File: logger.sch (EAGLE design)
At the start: 69 parts, among them IC1 LTC4412, J1 POWER_JACKPTH, Q1 FDN360P, Q2 FDN360P, Q3 2N7002PW, Q4 2N7002PW, U1 FT232RL

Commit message: Vcl attached to clock power and communication
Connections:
- new net D4-SENSE_3V3_SWITCH: MCU.PD4(XCK/T0), SENSE.EN, TPS6122.EN
- net D6-CLOCK_3V3_SWITCH: no longer MCU.PD4(XCK/T0), SENSE.EN, TPS6122.EN
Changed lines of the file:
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@@
 <net name="D6-CLOCK_3V3_SWITCH" class="0">
-<segment>
-<wire x1="152.4" y1="88.9" x2="185.42" y2="88.9" width="0.1524" layer="91"/>
-<label x="154.94" y="88.9" size="1.778" layer="95"/>
-<pinref part="MCU" gate="G$1" pin="PD4(XCK/T0)"/>
-</segment>
-<segment>
-<wire x1="116.84" y1="17.78" x2="116.84" y2="15.24" width="0.1524" layer="91"/>
-<wire x1="116.84" y1="15.24" x2="83.82" y2="15.24" width="0.1524" layer="91"/>
-<label x="83.82" y="15.24" size="1.778" layer="95"/>
-<pinref part="SENSE" gate="G$1" pin="EN"/>
-</segment>
 <segment>
 <wire x1="287.02" y1="256.54" x2="287.02" y2="254" width="0.1524" layer="91"/>
@@
 <label x="154.94" y="83.82" size="1.778" layer="95"/>
 <pinref part="MCU" gate="G$1" pin="PD6(AIN0)"/>
-</segment>
-<segment>
-<pinref part="TPS6122" gate="G$1" pin="EN"/>
-<wire x1="152.4" y1="-22.86" x2="147.32" y2="-22.86" width="0.1524" layer="91"/>
-<label x="147.32" y="-22.86" size="1.778" layer="95"/>
 </segment>
 </net>
@@
 </segment>
 </net>
+<net name="D4-SENSE_3V3_SWITCH" class="0">
+<segment>
+<pinref part="TPS6122" gate="G$1" pin="EN"/>
+<wire x1="147.32" y1="-22.86" x2="167.64" y2="-22.86" width="0.1524" layer="91"/>
+<label x="152.4" y="-22.86" size="1.778" layer="95"/>
+</segment>
+<segment>
+<pinref part="MCU" gate="G$1" pin="PD4(XCK/T0)"/>
+<wire x1="152.4" y1="88.9" x2="175.26" y2="88.9" width="0.1524" layer="91"/>
+<label x="154.94" y="88.9" size="1.778" layer="95"/>
+</segment>
+<segment>
+<pinref part="SENSE" gate="G$1" pin="EN"/>
+<wire x1="116.84" y1="17.78" x2="116.84" y2="15.24" width="0.1524" layer="91"/>
+<wire x1="116.84" y1="15.24" x2="86.36" y2="15.24" width="0.1524" layer="91"/>
+<label x="86.36" y="15.24" size="1.778" layer="95"/>
+</segment>
+</net>

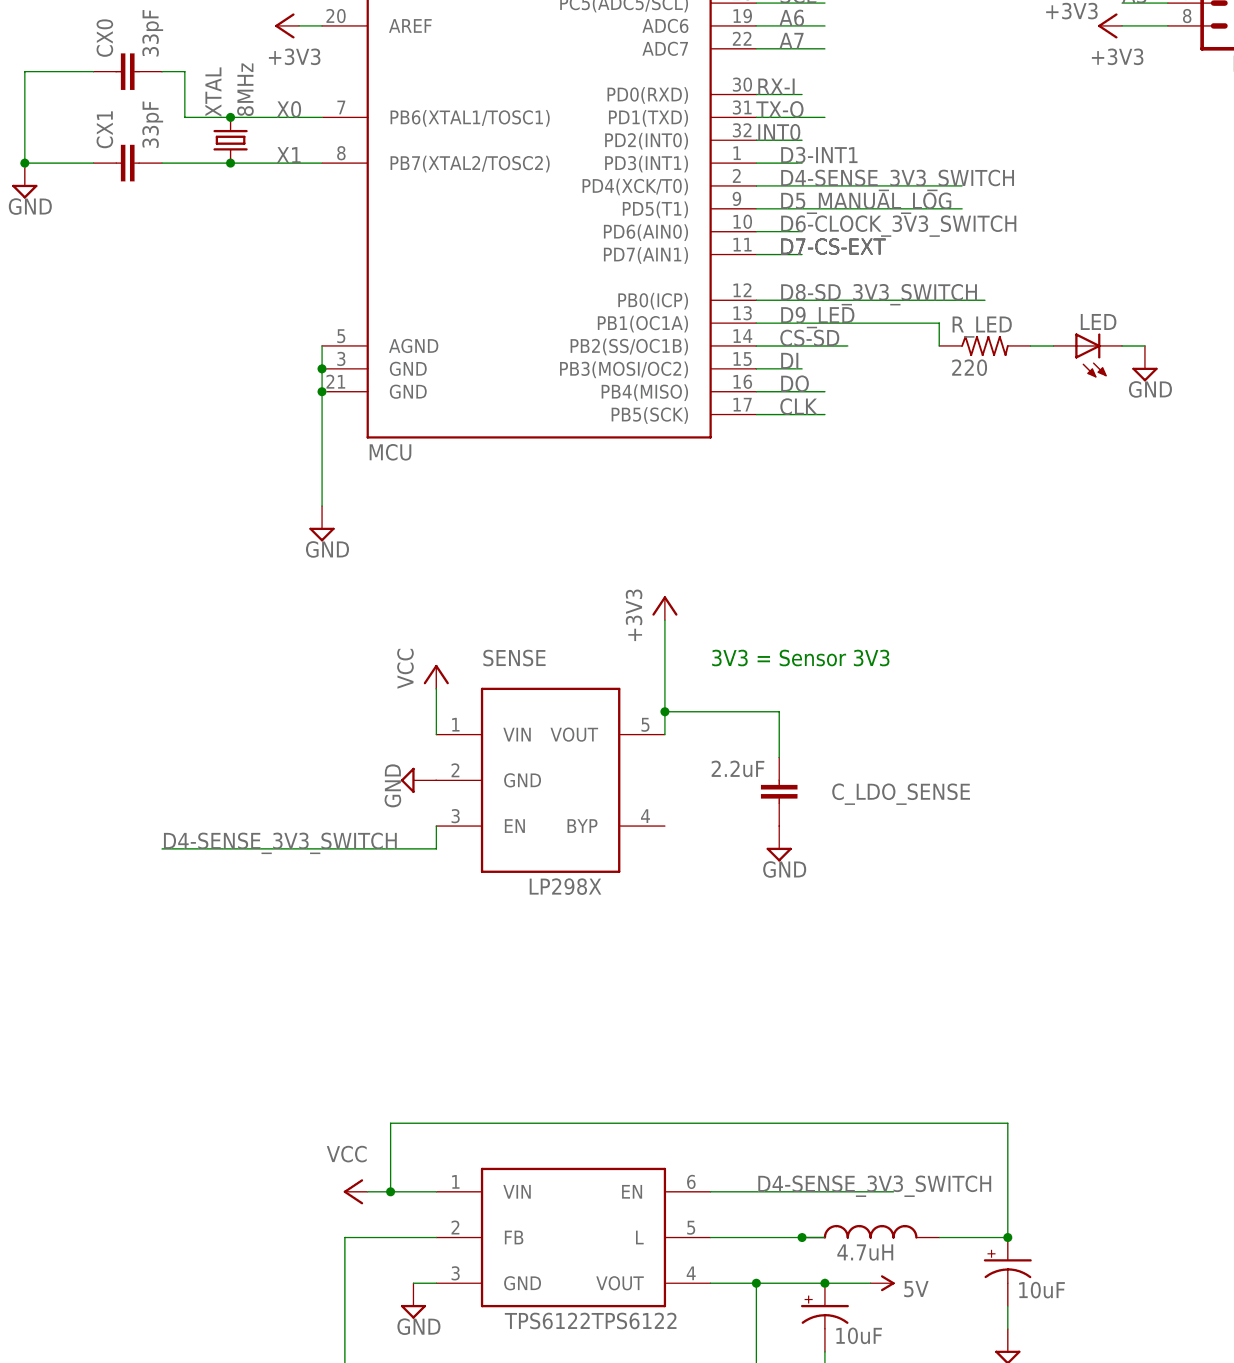
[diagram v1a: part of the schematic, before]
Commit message: Straighten traces
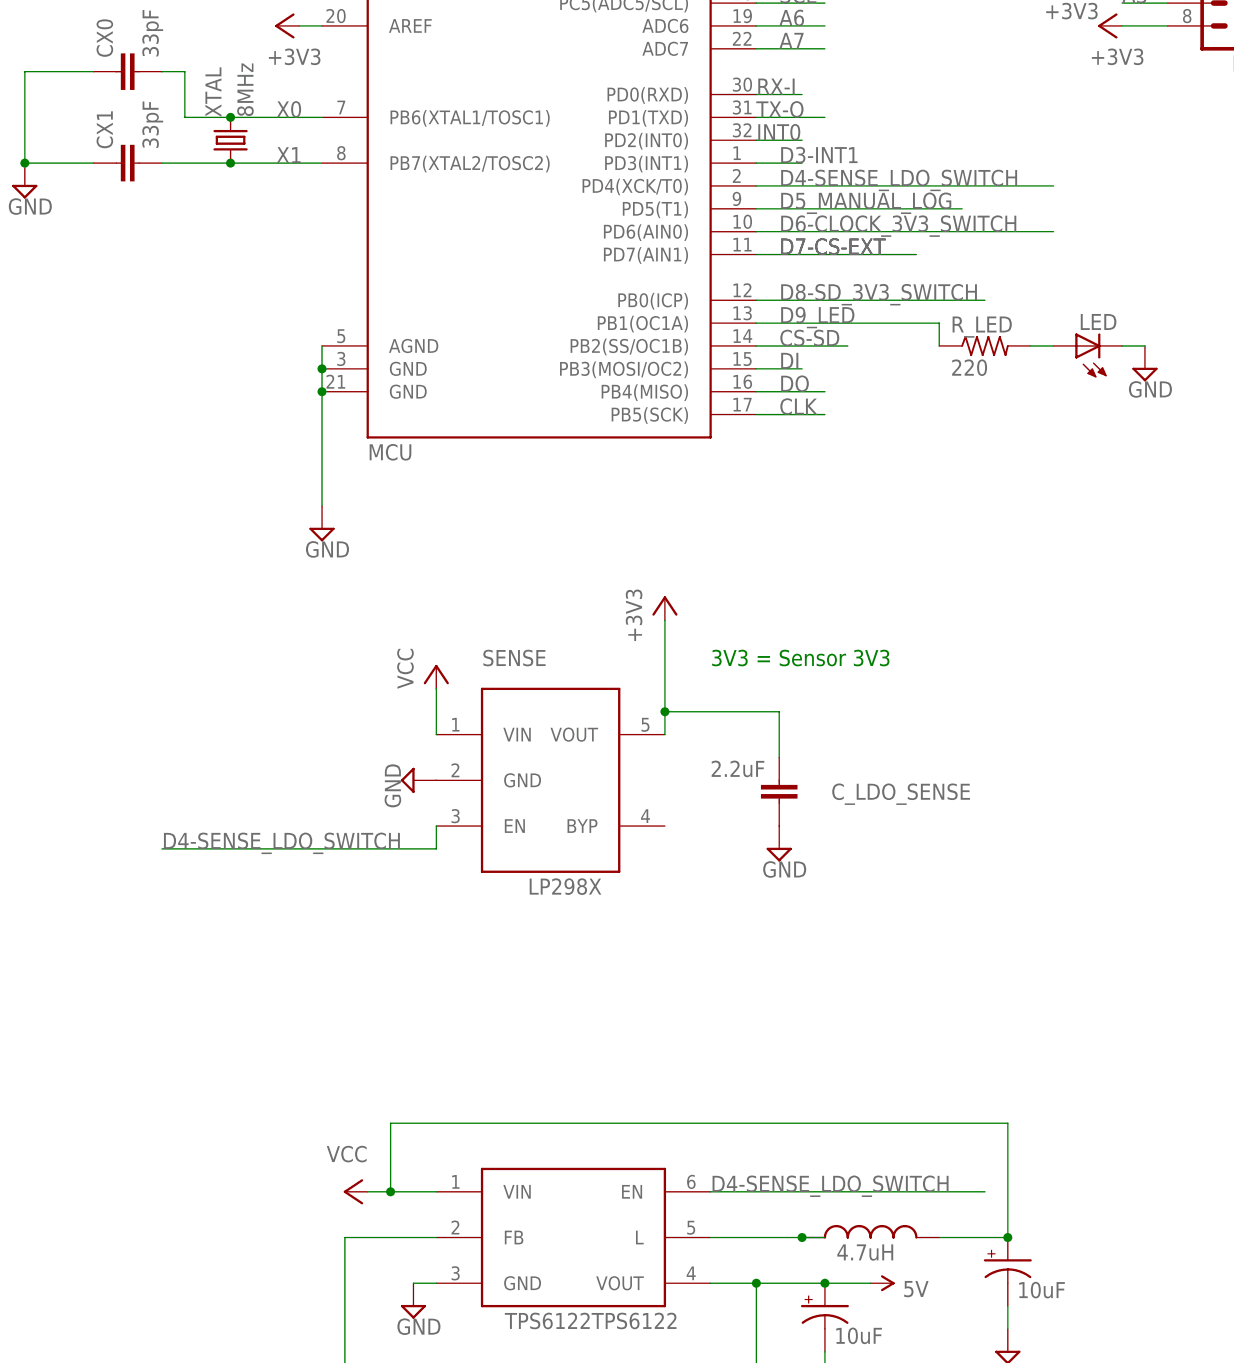
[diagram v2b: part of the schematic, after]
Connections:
- net D4-SENSE_3V3_SWITCH renamed D4-SENSE_LDO_SWITCH
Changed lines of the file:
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@@
 <net name="D7-CS-EXT" class="0">
 <segment>
-<wire x1="157.48" y1="81.28" x2="152.4" y2="81.28" width="0.1524" layer="91"/>
+<wire x1="170.18" y1="81.28" x2="152.4" y2="81.28" width="0.1524" layer="91"/>
 <label x="154.94" y="81.28" size="1.778" layer="95"/>
 <label x="154.94" y="81.28" size="1.778" layer="95"/>
@@
 </segment>
 <segment>
-<wire x1="152.4" y1="83.82" x2="157.48" y2="83.82" width="0.1524" layer="91"/>
+<wire x1="152.4" y1="83.82" x2="185.42" y2="83.82" width="0.1524" layer="91"/>
 <label x="154.94" y="83.82" size="1.778" layer="95"/>
 <pinref part="MCU" gate="G$1" pin="PD6(AIN0)"/>
@@
 </segment>
 </net>
-<net name="D4-SENSE_3V3_SWITCH" class="0">
+<net name="D4-SENSE_LDO_SWITCH" class="0">
 <segment>
 <pinref part="TPS6122" gate="G$1" pin="EN"/>
-<wire x1="147.32" y1="-22.86" x2="167.64" y2="-22.86" width="0.1524" layer="91"/>
-<label x="152.4" y="-22.86" size="1.778" layer="95"/>
+<wire x1="147.32" y1="-22.86" x2="177.8" y2="-22.86" width="0.1524" layer="91"/>
+<label x="147.32" y="-22.86" size="1.778" layer="95"/>
 </segment>
 <segment>
 <pinref part="MCU" gate="G$1" pin="PD4(XCK/T0)"/>
-<wire x1="152.4" y1="88.9" x2="175.26" y2="88.9" width="0.1524" layer="91"/>
+<wire x1="152.4" y1="88.9" x2="185.42" y2="88.9" width="0.1524" layer="91"/>
 <label x="154.94" y="88.9" size="1.778" layer="95"/>
 </segment>

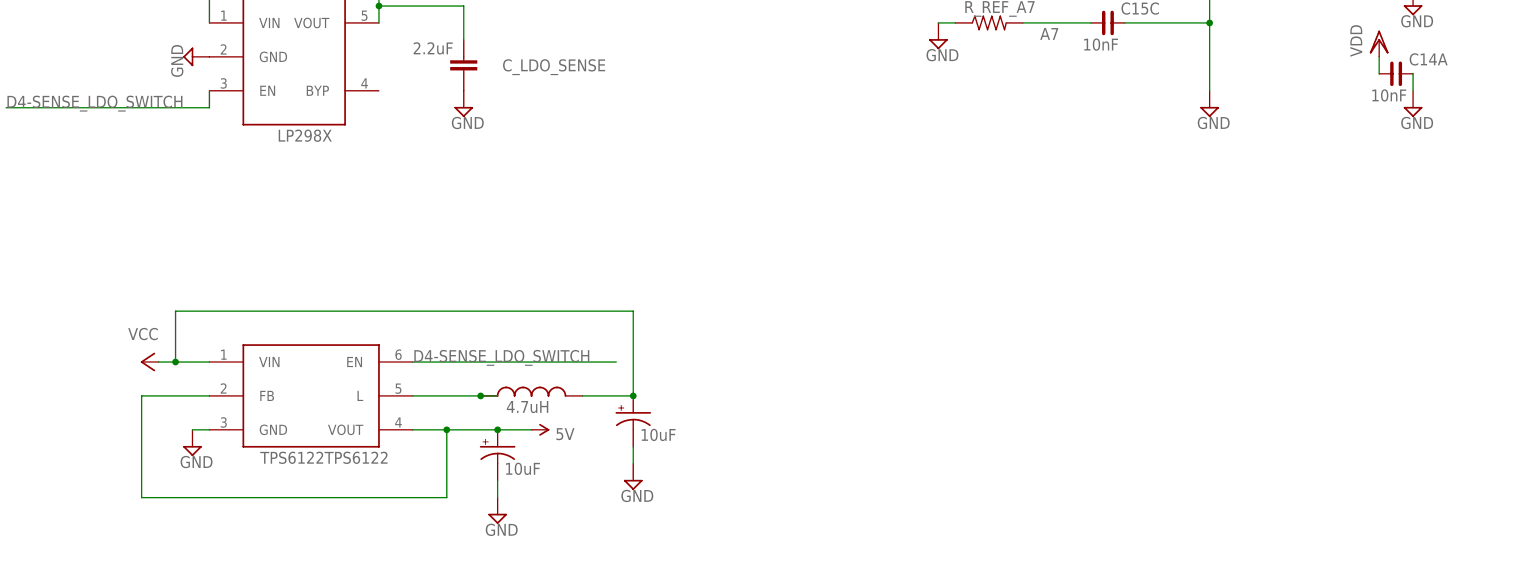
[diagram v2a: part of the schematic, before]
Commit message: Charge pump
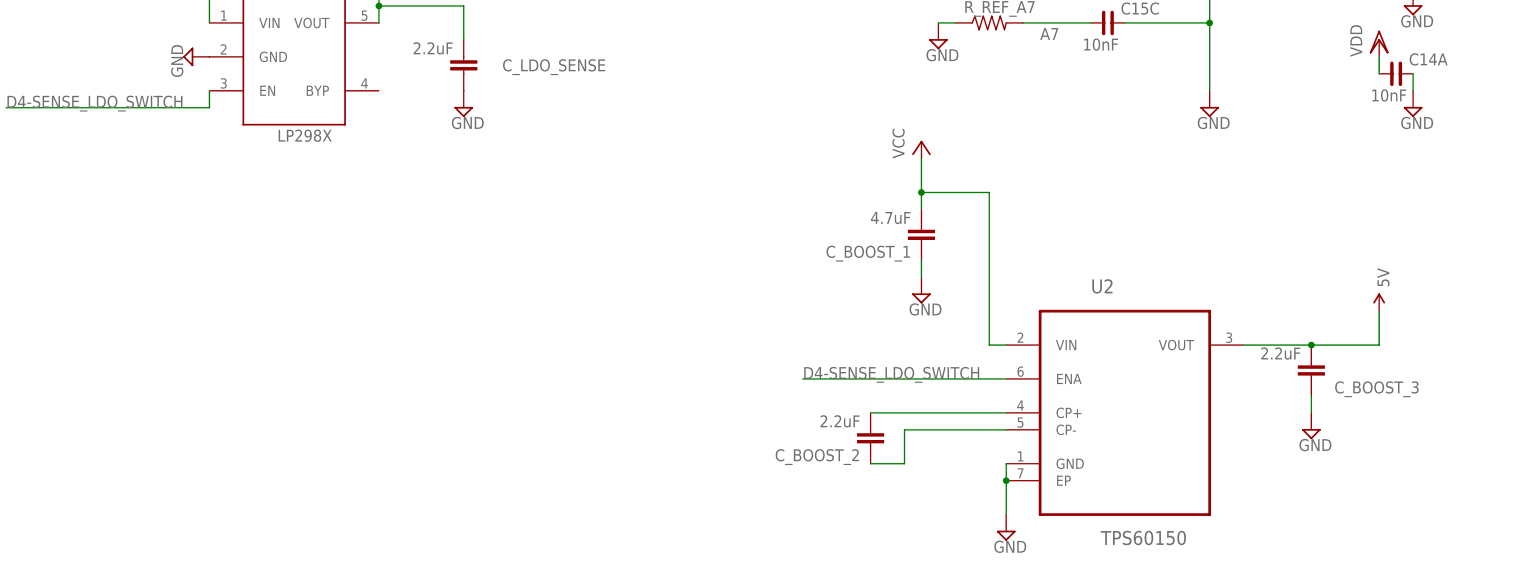
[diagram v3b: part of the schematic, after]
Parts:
- removed C1, C2: 10uF, SparkFun-Passives:CAP_POL1206
- removed L1: 4.7uH, SteveMarple:INDUCTOR1210
- removed TPS6122: TPS6122TPS6122, csandell:TPS6122TPS6122
- added C_BOOST_1: 4.7uF, resistor:C-EUC0603
- added C_BOOST_2, C_BOOST_3: 2.2uF, resistor:C-EUC0603
- added U2: TPS60150, ti_by_element14:TPS60150DRVR
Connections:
- removed net N$12: L1.1, TPS6122.L
- new net N$14: C_BOOST_2.2, U2.CP+
- new net N$15: C_BOOST_2.1, U2.CP-
- net 5V: now also C_BOOST_3.2, U2.VOUT; no longer C2.+, TPS6122.FB, TPS6122.VOUT
- net D4-SENSE_LDO_SWITCH: now also U2.ENA; no longer TPS6122.EN
- net GND: now also C_BOOST_1.1, C_BOOST_3.1, U2.EP, U2.GND; no longer C1.-, C2.-, TPS6122.GND
- net VCC: now also C_BOOST_1.2, U2.VIN; no longer C1.+, L1.2, TPS6122.VIN

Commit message: Updated BOM and board layout with cheaper and smaller component packages
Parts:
- removed C_LDO_SENSE1, DECOUP: 2.2uF, resistor:C-EUC0603
- removed RTC: DS3231SN, comfile:DS3231SN
- removed SENSE: LP2985, adafruit:LP298XS
- added 3.3_SENSE: LT1461DHS8-5PBF, LTC_By_element14_Batch_1:LT1461DHS8-5PBF
- added 5V_CHARGE_PUMP: TPS60150, ti_by_element14:TPS60150DRVR
- added C1: 0.1uF, resistor:C-EUC0603
- added CLOCK_BATT_DECOUPLE: 10uF, SparkFun-Passives:CAP_POL1206
- added CLOCK_CIN, SD_CIN, SENSE_CIN: 1uF, rcl:C-EUC0603
- added C_LDO_CLOCK: 2.2uF, resistor:C-EUC0603
- added D+, D-: 27ohm, rcl:R-US_R0603
- CLOCK_BATT_DECOUP: value 1uF -> 0.1uF
- MCU: value ATMega328 -> ATMEGA328P-MU; device SparkFun:ATMEGA168 -> Atmel_By_element14_Batch_1-00:ATMEGA328P-MU
- U1: value FT232RL -> DS3231MZ/V+T; device SparkFun-DigitalIC:FT232RL-BASICSSOP -> Maxim-DS3231MZ_8-SOIC:DS3231MZ/V+T
- U2: value TPS60150 -> FT231X-Q; device ti_by_element14:TPS60150DRVR -> FT231X:FT231X-Q
- renumbered R_REF_A0 to A0, R_REF_A1 to A1, R_REF_A2 to A2, R_REF_A3 to A3, R_REF_A6 to A6, R_REF_A7 to A7
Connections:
- new net N$13: D-.1, U2.USBDM
- new net N$16: D+.1, U2.USBDP
- new net N$17: C1.1, U2.3V3OUT, U2.RESET#, U2.VCCIO
- net +3V3: now also 3.3_SENSE.VOUT, H0.3, H0.5, H1.1, H1.3, H3.6; no longer H0.2, H0.4, H0.6, H0.8, H1.2, H1.4, H3.7, SENSE.VOUT
- net 5V: now also 5V_CHARGE_PUMP.VOUT, H3.7; no longer H3.6, U2.VOUT
- net A0: now also C14C.1, H0.2, MCU.PC0; no longer C15B.1, H0.1, MCU.PC0(ADC0)
- net A1: now also C14D.1, H0.4, MCU.PC1; no longer C15A.1, H0.3, MCU.PC1(ADC1)
- net A2: now also C15A.1, H0.6, MCU.PC2; no longer C14D.1, H0.5, MCU.PC2(ADC2)
- net A3: now also C15B.1, H0.8, MCU.PC3; no longer C14C.1, H0.7, MCU.PC3(ADC3)
- net A6: now also A6.1, C15C.2, H1.2; no longer A6.2, C15D.1, H1.1
- net A7: now also A7.1, C15D.2, H1.4; no longer A7.2, C15C.1, H1.3
- net BAT: now also CLOCK_BATT_DECOUPLE.+, U1.VBAT; no longer RTC.VBAT
- net CLK: now also MCU.PB5; no longer MCU.PB5(SCK)
- net CS-SD: now also MCU.PB2; no longer MCU.PB2(SS/OC1B)
- net D3-INT1: now also MCU.PD3; no longer MCU.PD3(INT1)
- net D4-SENSE_LDO_SWITCH: now also 3.3_SENSE.~SHDN, 5V_CHARGE_PUMP.ENA, MCU.PD4; no longer MCU.PD4(XCK/T0), SENSE.EN, U2.ENA
- net D5_MANUAL_LOG: now also MCU.PD5; no longer MCU.PD5(T1)
- net D6-CLOCK_3V3_SWITCH: now also MCU.PD6; no longer MCU.PD6(AIN0)
- net D7-CS-EXT: now also H3.5, MCU.PD7; no longer H3.4, MCU.PD7(AIN1)
- net D8-SD_3V3_SWITCH: now also MCU.PB0; no longer MCU.PB0(ICP)
- net D9_LED: now also MCU.PB1; no longer MCU.PB1(OC1A)
- net DI: now also MCU.PB3; no longer MCU.PB3(MOSI/OC2)
- net DO: now also MCU.PB4; no longer MCU.PB4(MISO)
- net DTR: now also U2.DTR#; no longer U1.DTR
- net GND: now also 3.3_SENSE.GND, 5V_CHARGE_PUMP.EP, 5V_CHARGE_PUMP.GND, A6.2, A7.2, C1.2, C15C.1, C15D.1, CLOCK_BATT_DECOUPLE.-, CLOCK_CIN.2, C_LDO_CLOCK.1, H0.1, H0.7, MCU.GND, MCU.GND_2, MCU.GND_3, SD_CIN.2, SENSE_CIN.2, U1.GND, U2.CTS#, U2.GND@13, U2.GND@21, U2.GND@3; no longer A6.1, A7.1, C15C.2, C15D.2, C_LDO_SENSE1.1, DECOUP.2, MCU.AGND, MCU.GND@1, MCU.GND@2, RTC.GND, RTC.NC1, RTC.NC2, RTC.NC3, RTC.NC4, RTC.NC5, RTC.NC6, RTC.NC7, RTC.NC8, SENSE.GND, U1.AGND, U1.CTS, U1.GND1, U1.GND2, U1.GND3, U1.TEST, U2.EP, U2.GND
- net INT0: now also MCU.PD2, U1.*INT/SQW; no longer MCU.PD2(INT0), RTC.!INT/SQW
- net N$14: now also 5V_CHARGE_PUMP.CP+; no longer U2.CP+
- net N$15: now also 5V_CHARGE_PUMP.CP-; no longer U2.CP-
- net N$27: now also U2.TXD; no longer U1.TXD
- net N$29: now also U2.RXD; no longer U1.RXD
- net N$3: now also D+.2; no longer U1.USBDP
- net N$4: now also D-.2; no longer U1.USBDM
- net N$5: now also U2.CBUS2; no longer U1.RXLED
- net N$6: now also U2.CBUS1; no longer U1.TXLED
- net RESET: now also MCU.PC6; no longer MCU.PC6(/RESET)
- net RX-I: now also MCU.PD0; no longer MCU.PD0(RXD)
- net SCL: now also MCU.PC5; no longer MCU.PC5(ADC5/SCL)
- net SCL_3V3: now also U1.SCL; no longer RTC.SCL
- net SDA: now also MCU.PC4; no longer MCU.PC4(ADC4/SDA)
- net SDA_3V3: now also U1.SDA; no longer RTC.SDA
- net TX-O: now also MCU.PD1; no longer MCU.PD1(TXD)
- net VCC: now also 3.3_SENSE.VIN, 5V_CHARGE_PUMP.VIN, C14A.1, CLOCK_CIN.1, H3.4, MCU.VCC, MCU.VCC_2, SD_CIN.1, SENSE_CIN.1; no longer C14B.1, DECOUP.1, H3.5, MCU.VCC@1, MCU.VCC@2, SENSE.VIN, U2.VIN
- net VCL: now also C_LDO_CLOCK.2, U1.VCC; no longer C_LDO_SENSE1.2, RTC.VCC
- net VDD: now also C14B.1; no longer C14A.1
- net VUSB: now also U2.VCC; no longer U1.VCC, U1.VCCIO
- net X0: now also MCU.PB6; no longer MCU.PB6(XTAL1/TOSC1)
- net X1: now also MCU.PB7; no longer MCU.PB7(XTAL2/TOSC2)
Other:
- moved on the sheet: ADECOUP, C14A, C14B, C14C, C14D, C15A, C15B, C15C, C15D, C17, C21, CLOCK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
